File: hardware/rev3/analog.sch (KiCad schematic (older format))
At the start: 53 parts, among them U4 LTC6409, U5 LTC6269, U6 AD9102, X1 DSC1123

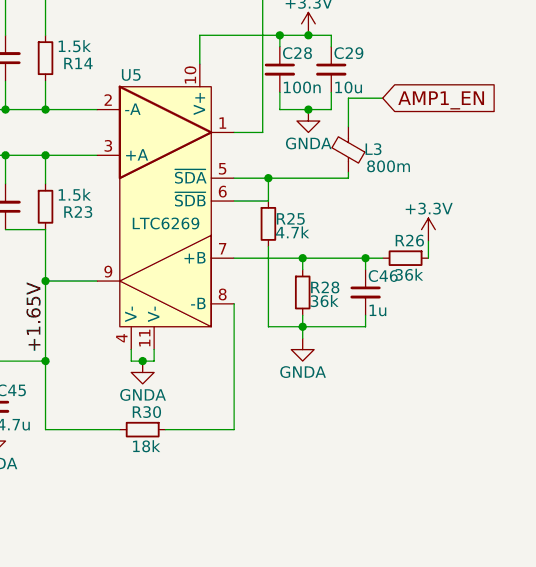
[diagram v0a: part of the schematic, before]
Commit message: Initial attempt at a complete layout.
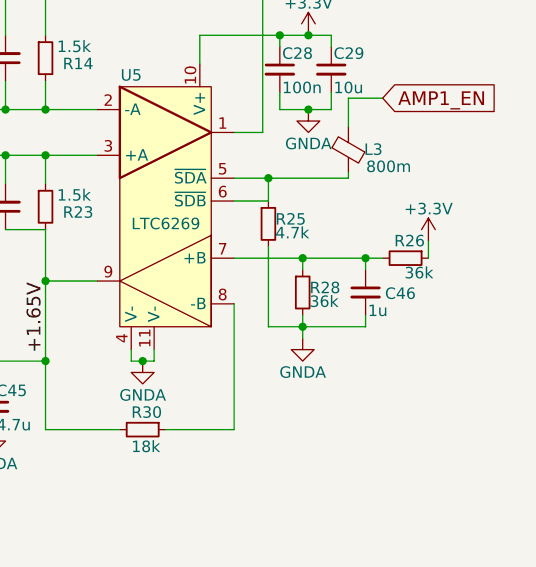
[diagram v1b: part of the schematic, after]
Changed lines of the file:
@@
 P 10700 3650
 F 0 "R26" V 10625 3600 50  0000 L CNN
-F 1 "36k" V 10775 3600 50  0000 L CNN
+F 1 "36k" V 10765 3645 50  0000 L CNN
 F 2 "Resistors_SMD:R_0603_HandSoldering" H 10700 3650 50  0001 C CNN
 F 3 "" H 10700 3650 50  0001 C CNN
@@
 U 1 1 59041C2E
 P 10525 3800
-F 0 "C46" H 10535 3870 50  0000 L CNN
+F 0 "C46" H 10610 3795 50  0000 L CNN
 F 1 "1u" H 10535 3720 50  0000 L CNN
 F 2 "Capacitors_SMD:C_0603_HandSoldering" H 10525 3800 50  0001 C CNN
